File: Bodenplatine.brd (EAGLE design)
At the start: 290 x 145 mm, 118 parts, among them K1 RY612012, K2 RY612012, K3 RY612012, K4 RY612012, K5 RY612012, K6 RY612012, K7 RY612012, K8 RY612012, K9 RY612012, Q1 BC846BLT1SMD, Q2 BC846BLT1SMD, Q3 BC846BLT1SMD, Q4 BC846BLT1SMD, Q5 BC846BLT1SMD, Q6 BC846BLT1SMD, Q7 BC846BLT1SMD, Q8 BC846BLT1SMD, Q9 BC846BLT1SMD, X1 SPRINGCON_AST125_5X2, X10 SPRINGCON_AST125_3X2, X11 SPRINGCON_AST125_4X2, X12 SPRINGCON_AST125_4X2, X13 SPRINGCON_AST125_5X2, X14 236-403, X15 236-402, X2 SPRINGCON_AST125_5X2, X3 SPRINGCON_AST125_5X2, X4 SPRINGCON_AST125_5X2, X5 SPRINGCON_AST125_5X2, X6 SPRINGCON_AST125_5X2, X7 SPRINGCON_AST125_5X2, X8 SPRINGCON_AST125_5X2, X9 SPRINGCON_AST125_5X2

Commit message: Import der Version v0.9.5
Aus dieser Version wurde der zweite Prototype erstellt. Der Produzent
war dieses Mal https://portal.multi-circuit-boards.eu
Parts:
- removed U$4: (no value), xMZ-Mod-Touch-Bodenplatine:LOGO_RA-GAS_BOTTOM
- added DRILEGEND: (no value), drilegend:DRILEGEND
- H1, H2, H3, H4: value MOUNT-HOLE3.3 -> MOUNT-PAD-ROUND3.3; device holes:3,3 -> holes:3,3-PAD
- U$5: device xMZ-Mod-Touch-Bodenplatine:LOGO_RA-GAS_BOTTOM -> xMZ-Mod-Touch-Bodenplatine:A3-LOC-RA-GAS
- moved U$5 112.1 mm to (135.9, 67.3), flipped to the top
- moved U$2 44.4 mm to (191.9, 125.9)
- moved U$3 35.6 mm to (191.8, 134.6)
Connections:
- removed net N$11: K2.A1, V6.C
- removed net N$17: K3.A1, V7.C
- removed net N$27: K4.A1, V8.C
- removed net N$37: K5.A1, V13.C
- removed net N$47: K6.A1, V14.C
- removed net N$57: K7.A1, V15.C
- removed net N$67: K8.A1, V16.C
- removed net N$77: K9.A1, V18.C
- removed net N$87: K1.A1, V5.C
- net 12V: now also K1.A1, K2.A1, K3.A1, K4.A1, K5.A1, K6.A1, K7.A1, K8.A1, K9.A1, V13.C, V14.C, V15.C, V16.C, V18.C, V5.C, V6.C, V7.C, V8.C
- net GND: now also H1.B3,3, H2.B3,3, H3.B3,3, H4.B3,3
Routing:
- net 12V: track 498.9 -> 875.8 mm
- net N$77: track 5.17 -> 0.00 mm
- net N$67: track 5.17 -> 0.00 mm
- net N$57: track 5.17 -> 0.00 mm
- net N$47: track 5.17 -> 0.00 mm
- net N$37: track 5.17 -> 0.00 mm
- net N$27: track 5.17 -> 0.00 mm
- net N$17: track 5.17 -> 0.00 mm
- net N$11: track 5.17 -> 0.00 mm
- net N$87: track 5.17 -> 0.00 mm
- net B+: track 269.2 -> 270.2 mm
- net A-: track 271.9 -> 272.9 mm
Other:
- outline, holes or cut-outs redrawn
- board text added: "0.00"
- board text added: "01-16"
- board text added: "100.00"
- board text added: "12V"
- board text added: "145.00"
- board text added: "15.00"
- board text added: "281.50"
- board text added: "290.00"
- board text added: "42.00"
- board text added: "58.00"
- board text added: "5V"
- board text added: "8.50"
- board text added: "All Dimensions in MM"
- board text added: "BOT"
- board text added: "FillOverPAD:GND:10:420"
- board text added: "FillOverPAD:GND:12:420"
- board text added: "FillOverPAD:GND:137:420"
- board text added: "FillOverPAD:GND:140:420"
- board text added: "FillOverPAD:GND:143:420"
- board text added: "FillOverPAD:GND:146:420"
- board text added: "FillOverPAD:GND:149:420"
- board text added: "FillOverPAD:GND:14:420"
- board text added: "FillOverPAD:GND:152:420"
- board text added: "FillOverPAD:GND:155:420"
- board text added: "FillOverPAD:GND:158:420"
- board text added: "FillOverPAD:GND:161:420"
- board text added: "FillOverPAD:GND:16:420"
- board text added: "FillOverPAD:GND:18:420"
- board text added: "FillOverPAD:GND:2:420"
- board text added: "FillOverPAD:GND:4:420"
- board text added: "FillOverPAD:GND:6:420"
- board text added: "FillOverPAD:GND:8:420"
- board text added: "LAYER-STACK"
- board text added: "P1"
- board text added: "P2"
- board text added: "P3"
- board text added: "P4"
- board text added: "P5"
- board text added: "P6"
- board text added: "P7"
- board text added: "P8"
- board text added: "P9"
- board text added: "TOP"

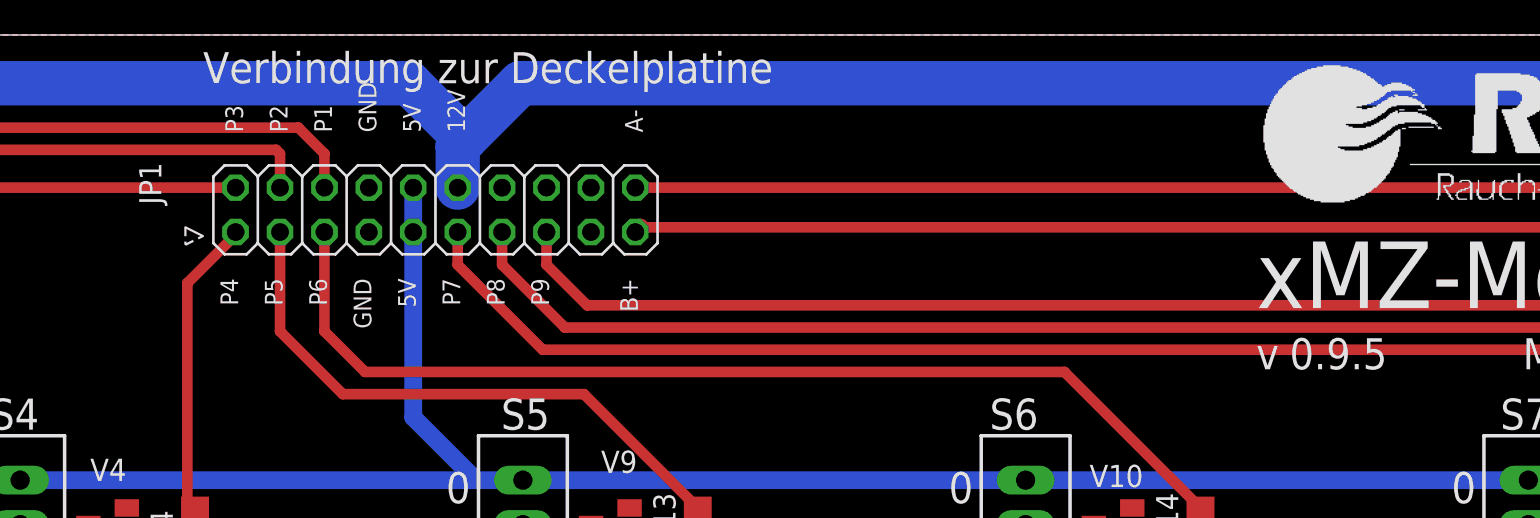
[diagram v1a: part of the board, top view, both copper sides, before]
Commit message: Anschluss Deckelplatine gegen verdrehen gesichert
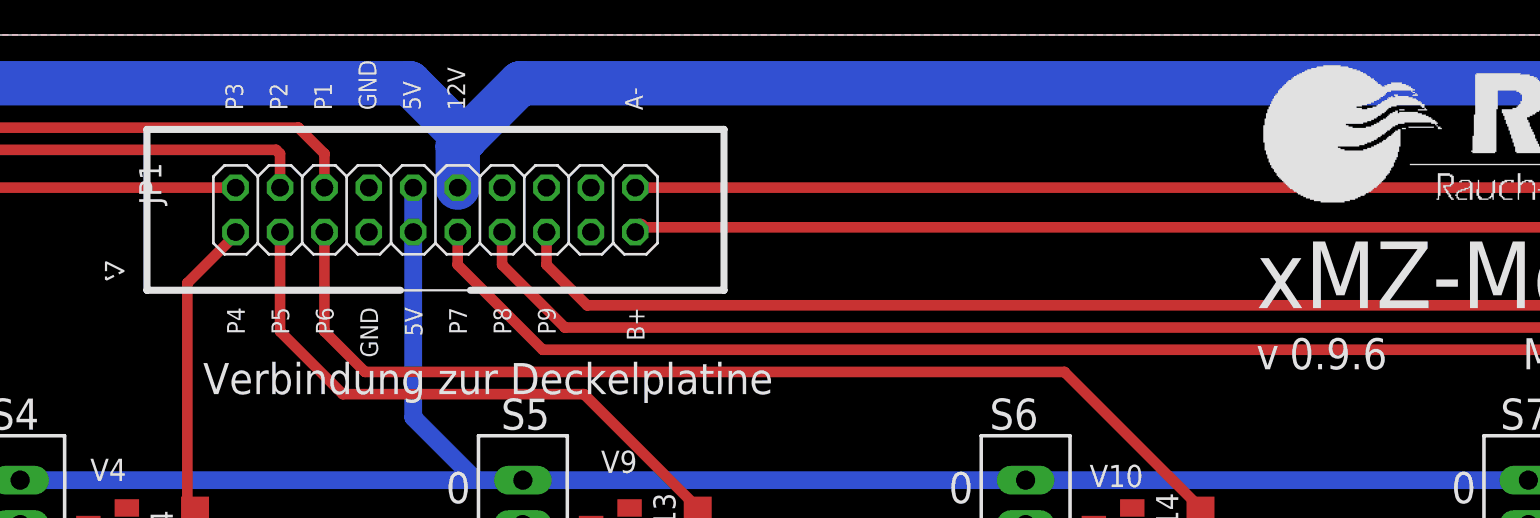
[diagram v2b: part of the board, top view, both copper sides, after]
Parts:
- JP1: device pinhead:2X10 -> xMZ-Mod-Touch-Bodenplatine:2X10
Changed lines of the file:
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@@
 <layer number="46" name="Milling" color="3" fill="1" visible="no" active="yes"/>
 <layer number="47" name="Measures" color="7" fill="1" visible="no" active="yes"/>
-<layer number="48" name="Document" color="7" fill="1" visible="yes" active="yes"/>
+<layer number="48" name="Document" color="7" fill="1" visible="no" active="yes"/>
 <layer number="49" name="Reference" color="7" fill="1" visible="no" active="yes"/>
 <layer number="50" name="dxf" color="7" fill="1" visible="no" active="no"/>
@@
 <text x="159.43" y="32.46" size="1.778" layer="21" font="vector" ratio="15">Stützklemme 12 Volt</text>
 <text x="239.72" y="31.94" size="1.778" layer="21" font="vector" ratio="15">BUS</text>
-<text x="131.71" y="144.018" size="1.778" layer="21" font="vector" ratio="15" align="top-left">Verbindung zur Deckelplatine</text>
+<text x="131.71" y="126.238" size="1.778" layer="21" font="vector" ratio="15" align="top-left">Verbindung zur Deckelplatine</text>
 <text x="44.704" y="144.018" size="1.778" layer="21" font="vector" ratio="15" align="top-left">12 Volt
 Spannungsversorgung BUS</text>
@@
 <text x="270.20625" y="106.1390625" size="0.05" layer="160" font="vector" ratio="15" rot="R10">FillOverPAD:GND:161:420</text>
 <wire x1="270.05" y1="106.1" x2="270.20625" y2="106.1390625" width="0.025" layer="160"/>
-<text x="132.7" y="131.08" size="1.016" layer="21" font="vector" rot="R270">P4</text>
-<text x="135.24" y="131.08" size="1.016" layer="21" font="vector" rot="R270">P5</text>
-<text x="137.78" y="131.08" size="1.016" layer="21" font="vector" rot="R270">P6</text>
-<text x="140.32" y="131.08" size="1.016" layer="21" font="vector" rot="R270">GND</text>
-<text x="142.86" y="131.08" size="1.016" layer="21" font="vector" rot="R270">5V</text>
-<text x="145.4" y="131.08" size="1.016" layer="21" font="vector" rot="R270">P7</text>
-<text x="147.94" y="131.08" size="1.016" layer="21" font="vector" rot="R270">P8</text>
-<text x="150.48" y="131.08" size="1.016" layer="21" font="vector" rot="R270">P9</text>
-<text x="155.56" y="131.08" size="1.016" layer="21" font="vector" rot="R270">B+</text>
-<text x="134" y="139.43" size="1.016" layer="21" font="vector" rot="R90">P3</text>
-<text x="136.54" y="139.43" size="1.016" layer="21" font="vector" rot="R90">P2</text>
-<text x="139.08" y="139.43" size="1.016" layer="21" font="vector" rot="R90">P1</text>
-<text x="141.62" y="139.43" size="1.016" layer="21" font="vector" rot="R90">GND</text>
-<text x="144.16" y="139.43" size="1.016" layer="21" font="vector" rot="R90">5V</text>
-<text x="146.7" y="139.43" size="1.016" layer="21" font="vector" rot="R90">12V</text>
-<text x="156.86" y="139.43" size="1.016" layer="21" font="vector" rot="R90">A-</text>
+<text x="133.081" y="129.429" size="1.016" layer="21" font="vector" rot="R270">P4</text>
+<text x="135.621" y="129.429" size="1.016" layer="21" font="vector" rot="R270">P5</text>
+<text x="138.161" y="129.429" size="1.016" layer="21" font="vector" rot="R270">P6</text>
+<text x="140.701" y="129.429" size="1.016" layer="21" font="vector" rot="R270">GND</text>
+<text x="143.241" y="129.429" size="1.016" layer="21" font="vector" rot="R270">5V</text>
+<text x="145.781" y="129.429" size="1.016" layer="21" font="vector" rot="R270">P7</text>
+<text x="148.321" y="129.429" size="1.016" layer="21" font="vector" rot="R270">P8</text>
+<text x="150.861" y="129.429" size="1.016" layer="21" font="vector" rot="R270">P9</text>
+<text x="155.941" y="129.429" size="1.016" layer="21" font="vector" rot="R270">B+</text>
+<text x="134" y="140.7" size="1.016" layer="21" font="vector" rot="R90">P3</text>
+<text x="136.54" y="140.7" size="1.016" layer="21" font="vector" rot="R90">P2</text>
+<text x="139.08" y="140.7" size="1.016" layer="21" font="vector" rot="R90">P1</text>
+<text x="141.62" y="140.7" size="1.016" layer="21" font="vector" rot="R90">GND</text>
+<text x="144.16" y="140.7" size="1.016" layer="21" font="vector" rot="R90">5V</text>
+<text x="146.7" y="140.7" size="1.016" layer="21" font="vector" rot="R90">12V</text>
+<text x="156.86" y="140.7" size="1.016" layer="21" font="vector" rot="R90">A-</text>
 <text x="290" y="-13" size="1.77" layer="47" font="vector" rot="R90">290.00</text>
 <wire x1="290" y1="-1.27" x2="290" y2="-22.99" width="0.2" layer="47"/>
@@
 <attribute name="DESCRIPTION" value=""/>
 <attribute name="PROJEKTNAME" value="xMZ-Mod-Touch-Bodenplatine"/>
-<attribute name="VERSION" value="0.9.5"/>
+<attribute name="VERSION" value="0.9.6"/>
 </attributes>
 <variantdefs>
@@
 <attribute name="MPN" value="" x="45" y="18" size="1.778" layer="27" display="off"/>
 </element>
-<element name="JP1" library="pinhead" package="2X10" value="Stiftleiste 2x20 pol" x="145" y="135" smashed="yes">
+<element name="JP1" library="xMZ-Mod-Touch-Bodenplatine" package="2X10" value="Stiftleiste 2x20 pol" x="145" y="135" smashed="yes">
 <attribute name="OC_FARNELL" value="3417773" x="145" y="135" size="1.778" layer="27" display="off"/>
 <attribute name="MF" value="TE CONNECTIVITY / AMP" x="145" y="135" size="1.778" layer="27" display="off"/>
